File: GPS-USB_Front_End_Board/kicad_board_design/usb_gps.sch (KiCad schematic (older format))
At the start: 1 part, among them P1 CONN_02X12

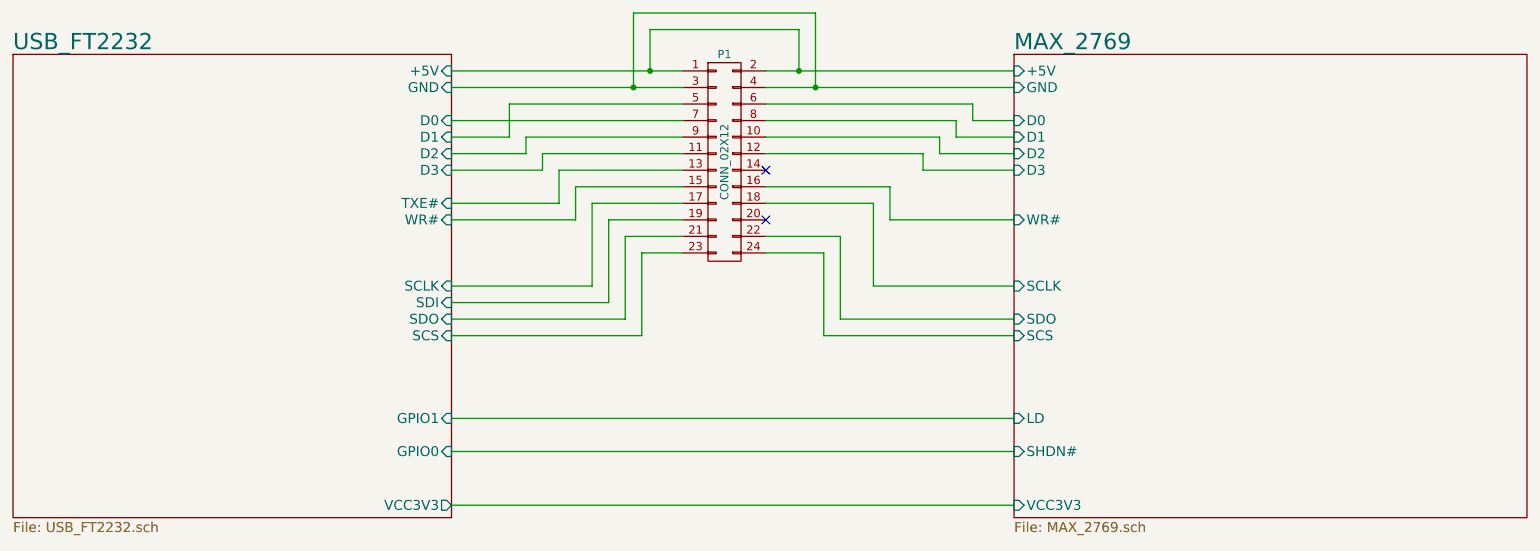
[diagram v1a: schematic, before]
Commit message: Change SMA footprint, add SAW filter, extend header pins.
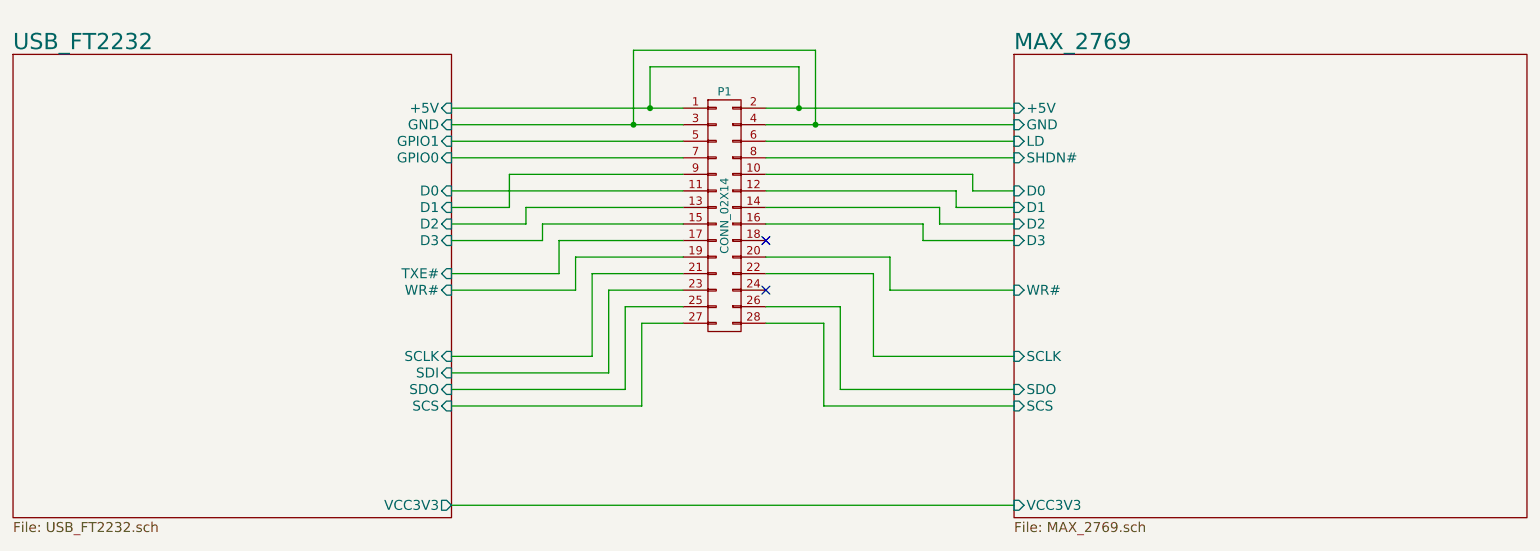
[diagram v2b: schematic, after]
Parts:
- removed P1: CONN_02X12, Pin_Headers:Pin_Header_Straight_2x12, symbol CONN_02X12
- added P1: CONN_02X14, Pin_Headers:Pin_Header_Straight_2x14, symbol CONN_02X14
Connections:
- net MAX_2769/+5V: now also P1.1 (P1), P1.2 (P2)
- net MAX_2769/D0: now also P1.10 (P10)
- net MAX_2769/D1: now also P1.12 (P12)
- net MAX_2769/D2: now also P1.14 (P14)
- net MAX_2769/D3: now also P1.16 (P16)
- net MAX_2769/GND: now also P1.3 (P3), P1.4 (P4)
- net MAX_2769/LD: now also P1.6 (P6)
- net MAX_2769/SCLK: now also P1.22 (P22)
- net MAX_2769/SCS: now also P1.28 (P28)
- net MAX_2769/SDO: now also P1.26 (P26)
- net MAX_2769/SHDN#: now also P1.8 (P8)
- net MAX_2769/WR#: now also P1.20 (P20)
- net USB_FT2232/D0: now also P1.11 (P11)
- net USB_FT2232/D1: now also P1.9 (P9)
- net USB_FT2232/D2: now also P1.13 (P13)
- net USB_FT2232/D3: now also P1.15 (P15)
- net USB_FT2232/SCLK: now also P1.21 (P21)
- net USB_FT2232/SCS: now also P1.27 (P27)
- net USB_FT2232/SDI: now also P1.23 (P23)
- net USB_FT2232/SDO: now also P1.25 (P25)
- net USB_FT2232/TXE#: now also P1.17 (P17)
- net USB_FT2232/WR#: now also P1.19 (P19)
- new net USB_FT2232/GPIO0: P1.7 (P7)
- new net USB_FT2232/GPIO1: P1.5 (P5)
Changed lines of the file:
@@
 F0 "USB_FT2232" 98
 F1 "USB_FT2232.sch" 60
-F2 "D0" I R 3600 3100 60
-F3 "D1" I R 3600 3200 60
-F4 "D2" I R 3600 3300 60
-F5 "D3" I R 3600 3400 60
-F6 "TXE#" I R 3600 3600 60
-F7 "WR#" I R 3600 3700 60
-F8 "SCLK" I R 3600 4100 60
-F9 "SDO" I R 3600 4300 60
-F10 "SCS" I R 3600 4400 60
-F11 "+5V" I R 3600 2800 60
-F12 "GND" I R 3600 2900 60
-F13 "SDI" I R 3600 4200 60
-F14 "GPIO1" I R 3600 4900 60
-F15 "GPIO0" I R 3600 5100 60
+F2 "D0" I R 3600 3525 60
+F3 "D1" I R 3600 3625 60
+F4 "D2" I R 3600 3725 60
+F5 "D3" I R 3600 3825 60
+F6 "TXE#" I R 3600 4025 60
+F7 "WR#" I R 3600 4125 60
+F8 "SCLK" I R 3600 4525 60
+F9 "SDO" I R 3600 4725 60
+F10 "SCS" I R 3600 4825 60
+F11 "+5V" I R 3600 3025 60
+F12 "GND" I R 3600 3125 60
+F13 "SDI" I R 3600 4625 60
+F14 "GPIO1" I R 3600 3225 60
+F15 "GPIO0" I R 3600 3325 60
 F16 "VCC3V3" O R 3600 5425 60
 $EndSheet
@@
 F0 "MAX_2769" 98
 F1 "MAX_2769.sch" 60
-F2 "+5V" I L 7000 2800 60
-F3 "GND" I L 7000 2900 60
-F4 "SCLK" I L 7000 4100 60
-F5 "SDO" I L 7000 4300 60
-F6 "WR#" I L 7000 3700 60
-F7 "D0" I L 7000 3100 60
-F8 "D1" I L 7000 3200 60
-F9 "D2" I L 7000 3300 60
-F10 "D3" I L 7000 3400 60
-F11 "SCS" I L 7000 4400 60
-F12 "LD" I L 7000 4900 60
-F13 "SHDN#" I L 7000 5100 60
+F2 "+5V" I L 7000 3025 60
+F3 "GND" I L 7000 3125 60
+F4 "SCLK" I L 7000 4525 60
+F5 "SDO" I L 7000 4725 60
+F6 "WR#" I L 7000 4125 60
+F7 "D0" I L 7000 3525 60
+F8 "D1" I L 7000 3625 60
+F9 "D2" I L 7000 3725 60
+F10 "D3" I L 7000 3825 60
+F11 "SCS" I L 7000 4825 60
+F12 "LD" I L 7000 3225 60
+F13 "SHDN#" I L 7000 3325 60
 F14 "VCC3V3" I L 7000 5425 60
 $EndSheet
+NoConn ~ 5500 3825
+NoConn ~ 5500 4125
+Wire Wire Line
+	3600 3525 5000 3525
+Wire Wire Line
+	3600 3625 3950 3625
+Wire Wire Line
+	3600 3725 4050 3725
+Wire Wire Line
+	3600 3825 4150 3825
+Wire Wire Line
+	4150 3825 4150 3725
+Wire Wire Line
+	4150 3725 5000 3725
+Wire Wire Line
+	3600 4025 4250 4025
+Wire Wire Line
+	4250 4025 4250 3825
+Wire Wire Line
+	4250 3825 5000 3825
+Wire Wire Line
+	3600 4125 4350 4125
+Wire Wire Line
+	4350 4125 4350 3925
+Wire Wire Line
+	4350 3925 5000 3925
+Wire Wire Line
+	3600 4525 4450 4525
+Wire Wire Line
+	4450 4525 4450 4025
+Wire Wire Line
+	4450 4025 5000 4025
+Wire Wire Line
+	3600 4625 4550 4625
+Wire Wire Line
+	4550 4625 4550 4125
+Wire Wire Line
+	4550 4125 5000 4125
+Wire Wire Line
+	3600 4725 4650 4725
+Wire Wire Line
+	4650 4725 4650 4225
+Wire Wire Line
+	4650 4225 5000 4225
+Wire Wire Line
+	3600 4825 4750 4825
+Wire Wire Line
+	4750 4825 4750 4325
+Wire Wire Line
+	4750 4325 5000 4325
+Wire Wire Line
+	7000 3525 6750 3525
+Wire Wire Line
+	6750 3525 6750 3425
+Wire Wire Line
+	6750 3425 5500 3425
+Wire Wire Line
+	7000 3625 6650 3625
+Wire Wire Line
+	6650 3625 6650 3525
+Wire Wire Line
+	6650 3525 5500 3525
+Wire Wire Line
+	7000 3725 6550 3725
+Wire Wire Line
+	6550 3725 6550 3625
+Wire Wire Line
+	6550 3625 5500 3625
+Wire Wire Line
+	7000 3825 6450 3825
+Wire Wire Line
+	6450 3825 6450 3725
+Wire Wire Line
+	6450 3725 5500 3725
+Wire Wire Line
+	7000 4125 6250 4125
+Wire Wire Line
+	6250 4125 6250 3925
+Wire Wire Line
+	6250 3925 5500 3925
+Wire Wire Line
+	7000 4525 6150 4525
+Wire Wire Line
+	6150 4525 6150 4025
+Wire Wire Line
+	6150 4025 5500 4025
+Wire Wire Line
+	7000 4725 5950 4725
+Wire Wire Line
+	5950 4725 5950 4225
+Wire Wire Line
+	5950 4225 5500 4225
+Wire Wire Line
+	7000 4825 5850 4825
+Wire Wire Line
+	5850 4825 5850 4325
+Wire Wire Line
+	5850 4325 5500 4325
+Wire Wire Line
+	4050 3725 4050 3625
+Wire Wire Line
+	4050 3625 5000 3625
+Wire Wire Line
+	3950 3625 3950 3425
+Wire Wire Line
+	3950 3425 5000 3425
+Wire Wire Line
+	3600 3125 5000 3125
+Wire Wire Line
+	5500 3125 7000 3125
+Wire Wire Line
+	4700 3125 4700 2675
+Wire Wire Line
+	4700 2675 5800 2675
+Wire Wire Line
+	5800 2675 5800 3125
+Connection ~ 5800 3125
+Connection ~ 4700 3125
+Wire Wire Line
+	3600 3025 5000 3025
+Wire Wire Line
+	5500 3025 7000 3025
+Wire Wire Line
+	4800 3025 4800 2775
+Wire Wire Line
+	4800 2775 5700 2775
+Wire Wire Line
+	5700 2775 5700 3025
+Connection ~ 5700 3025
+Connection ~ 4800 3025
+Wire Wire Line
+	3600 5425 7000 5425
 $Comp
-L CONN_02X12 P1
-U 1 1 5B265B59
-P 5250 3350
-F 0 "P1" H 5250 4000 50  0000 C CNN
-F 1 "CONN_02X12" V 5250 3350 50  0000 C CNN
-F 2 "Pin_Headers:Pin_Header_Straight_2x12" H 5250 2150 50  0001 C CNN
-F 3 "" H 5250 2150 50  0000 C CNN
-F 4 "Sullins" H 5250 3350 60  0001 C CNN "MFR"
-F 5 "SFH11-PBPC-D12-ST-BK" H 5250 3350 60  0001 C CNN "MPN"
-F 6 "Digikey" H 5250 3350 60  0001 C CNN "SPR"
-F 7 "S9708-ND" H 5250 3350 60  0001 C CNN "SPN"
-	1    5250 3350
+L CONN_02X14 P1
+U 1 1 5DBDA58D
+P 5250 3675
+F 0 "P1" H 5250 4425 50  0000 C CNN
+F 1 "CONN_02X14" V 5250 3675 50  0000 C CNN
+F 2 "Pin_Headers:Pin_Header_Straight_2x14" H 5250 2525 50  0001 C CNN
+F 3 "" H 5250 2525 50  0000 C CNN
+F 4 "Sullins" H 5250 3675 60  0001 C CNN "MFR"
+F 5 "PPTC142LFBN-RC" H 5250 3675 60  0001 C CNN "MPN"
+F 6 "Digikey" H 5250 3675 60  0001 C CNN "SPR"
+F 7 "S7082-ND" H 5250 3675 60  0001 C CNN "SPN"
+	1    5250 3675
 	1    0    0    -1
 $EndComp
-NoConn ~ 5500 3400
-NoConn ~ 5500 3700
 Wire Wire Line
-	3600 3100 5000 3100
+	3600 3325 5000 3325
 Wire Wire Line
-	3600 3200 3950 3200
+	5500 3325 7000 3325
 Wire Wire Line
-	3600 3300 4050 3300
+	3600 3225 5000 3225
 Wire Wire Line
-	3600 3400 4150 3400
-Wire Wire Line
-	4150 3400 4150 3300
-Wire Wire Line
-	4150 3300 5000 3300
-Wire Wire Line
-	3600 3600 4250 3600
-Wire Wire Line
-	4250 3600 4250 3400
-Wire Wire Line
-	4250 3400 5000 3400
-Wire Wire Line
-	3600 3700 4350 3700
-Wire Wire Line
-	4350 3700 4350 3500
-Wire Wire Line
-	4350 3500 5000 3500
-Wire Wire Line
-	3600 4100 4450 4100
-Wire Wire Line
-	4450 4100 4450 3600
-Wire Wire Line
-	4450 3600 5000 3600
-Wire Wire Line
-	3600 4200 4550 4200
-Wire Wire Line
-	4550 4200 4550 3700
-Wire Wire Line
-	4550 3700 5000 3700
-Wire Wire Line
-	3600 4300 4650 4300
-Wire Wire Line
-	4650 4300 4650 3800
-Wire Wire Line
-	4650 3800 5000 3800
-Wire Wire Line
-	3600 4400 4750 4400
-Wire Wire Line
-	4750 4400 4750 3900
-Wire Wire Line
-	4750 3900 5000 3900
-Wire Wire Line
-	7000 3100 6750 3100
-Wire Wire Line
-	6750 3100 6750 3000
-Wire Wire Line
-	6750 3000 5500 3000
-Wire Wire Line
-	7000 3200 6650 3200
-Wire Wire Line
-	6650 3200 6650 3100
-Wire Wire Line
-	6650 3100 5500 3100
-Wire Wire Line
-	7000 3300 6550 3300
-Wire Wire Line
-	6550 3300 6550 3200
-Wire Wire Line
-	6550 3200 5500 3200
-Wire Wire Line
-	7000 3400 6450 3400
-Wire Wire Line
-	6450 3400 6450 3300
-Wire Wire Line
-	6450 3300 5500 3300
-Wire Wire Line
-	7000 3700 6250 3700
-Wire Wire Line
-	6250 3700 6250 3500
-Wire Wire Line
-	6250 3500 5500 3500
-Wire Wire Line
-	7000 4100 6150 4100
-Wire Wire Line
-	6150 4100 6150 3600
-Wire Wire Line
-	6150 3600 5500 3600
-Wire Wire Line
-	7000 4300 5950 4300
-Wire Wire Line
-	5950 4300 5950 3800
-Wire Wire Line
-	5950 3800 5500 3800
-Wire Wire Line
-	7000 4400 5850 4400
-Wire Wire Line
-	5850 4400 5850 3900
-Wire Wire Line
-	5850 3900 5500 3900
-Wire Wire Line
-	3600 4900 7000 4900
-Wire Wire Line
-	3600 5100 7000 5100
-Wire Wire Line
-	4050 3300 4050 3200
-Wire Wire Line
-	4050 3200 5000 3200
-Wire Wire Line
-	3950 3200 3950 3000
-Wire Wire Line
-	3950 3000 5000 3000
-Wire Wire Line
-	3600 2900 5000 2900
-Wire Wire Line
-	5500 2900 7000 2900
-Wire Wire Line
-	4700 2900 4700 2450
-Wire Wire Line
-	4700 2450 5800 2450
-Wire Wire Line
-	5800 2450 5800 2900
-Connection ~ 5800 2900
-Connection ~ 4700 2900
-Wire Wire Line
-	3600 2800 5000 2800
-Wire Wire Line
-	5500 2800 7000 2800
-Wire Wire Line
-	4800 2800 4800 2550
-Wire Wire Line
-	4800 2550 5700 2550
-Wire Wire Line
-	5700 2550 5700 2800
-Connection ~ 5700 2800
-Connection ~ 4800 2800
-Wire Wire Line
-	3600 5425 7000 5425
+	5500 3225 7000 3225
 $EndSCHEMATC

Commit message: Add LED P/N.  Process BOM prior to order.
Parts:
- P1: SPURL (none) -> -
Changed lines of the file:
@@
 $EndDescr
 $Sheet
-S 950  2700 2650 2800
+S 950 2700 2650 2800
 U 5B1BC185
 F0 "USB_FT2232" 98
@@
 F14 "VCC3V3" I L 7000 5425 60
 $EndSheet
-NoConn ~ 5500 3825
-NoConn ~ 5500 4125
+$Comp
+L CONN_02X14 P1
+U 1 1 5DBDA58D
+P 5250 3675
+F 0 "P1" H 5250 4425 50 0000 C CNN
+F 1 "CONN_02X14" V 5250 3675 50 0000 C CNN
+F 2 "Pin_Headers:Pin_Header_Straight_2x14" H 5250 2525 50 0001 C CNN
+F 3 "" H 5250 2525 50 0000 C CNN
+F 4 "Sullins" H 5250 3675 60 0001 C CNN "MFR"
+F 5 "PPTC142LFBN-RC" H 5250 3675 60 0001 C CNN "MPN"
+F 6 "Digikey" H 5250 3675 60 0001 C CNN "SPR"
+F 7 "S7082-ND" H 5250 3675 60 0001 C CNN "SPN"
+F 8 "-" H 0 0 50 0001 C CNN "SPURL"
+	1    5250 3675
+	1    0    0    -1
+$EndComp
 Wire Wire Line
 	3600 3525 5000 3525
@@
 Wire Wire Line
 	5800 2675 5800 3125
-Connection ~ 5800 3125
-Connection ~ 4700 3125
 Wire Wire Line
 	3600 3025 5000 3025
@@
 Wire Wire Line
 	5700 2775 5700 3025
-Connection ~ 5700 3025
-Connection ~ 4800 3025
 Wire Wire Line
 	3600 5425 7000 5425
-$Comp
-L CONN_02X14 P1
-U 1 1 5DBDA58D
-P 5250 3675
-F 0 "P1" H 5250 4425 50  0000 C CNN
-F 1 "CONN_02X14" V 5250 3675 50  0000 C CNN
-F 2 "Pin_Headers:Pin_Header_Straight_2x14" H 5250 2525 50  0001 C CNN
-F 3 "" H 5250 2525 50  0000 C CNN
-F 4 "Sullins" H 5250 3675 60  0001 C CNN "MFR"
-F 5 "PPTC142LFBN-RC" H 5250 3675 60  0001 C CNN "MPN"
-F 6 "Digikey" H 5250 3675 60  0001 C CNN "SPR"
-F 7 "S7082-ND" H 5250 3675 60  0001 C CNN "SPN"
-	1    5250 3675
-	1    0    0    -1
-$EndComp
 Wire Wire Line
 	3600 3325 5000 3325
@@
 Wire Wire Line
 	5500 3225 7000 3225
+Connection ~ 5800 3125
+Connection ~ 4700 3125
+Connection ~ 5700 3025
+Connection ~ 4800 3025
+NoConn ~ 5500 3825
+NoConn ~ 5500 4125
 $EndSCHEMATC
